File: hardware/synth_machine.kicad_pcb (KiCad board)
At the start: 2 copper layers, 100 x 100 mm, 93 parts, among them J1 USB-C (MIDI + 5V power), J10 Pot WAV (10k lin, panel) JST-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, J11 Pot ATK (10k lin, panel) JST-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, J12 Pot DEC (10k lin, panel) JST-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, J13 Pot SUS (10k lin, panel) JST-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, J14 Pot REL (10k lin, panel) JST-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, J5 Speaker L (JST-PH), J6 Speaker R (JST-PH), J7 Headphones 3.5mm (CUI SJ1-351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, J8 Expansion, K1 KEY C4 (direct D10) JST-XH, K10 A4 [c2 r2] JST-XH, K11 A#4 [c1 r1] JST-XH, K12 B4 [c1 r2] JST-XH, K13 C5 [c0 r2] JST-XH, K14 BTN1 [c0 r0] JST-XH, K15 BTN2 [c0 r1] JST-XH, K16 BTN3 [c1 r0] JST-XH, K17 BTN4 [c2 r0] JST-XH, K18 BTN5 [c3 r0] JST-XH, K19 BTN6 [c4 r0] JST-XH, K2 C#4 [c5 r0] JST-XH, K3 D4 [c5 r1] JST-XH, K4 D#4 [c4 r1] JST-XH, K5 E4 [c5 r2] JST-XH, K6 F4 [c4 r2] JST-XH, K7 F#4 [c3 r1] JST-XH, K8 G4 [c3 r2] JST-XH, K9 G#4 [c2 r1] JST-XH, Q1 MMBT3904, U1 Daisy Seed / Seed3, U2 TPA6138A2PWR, U3 MAX98306ETD+T

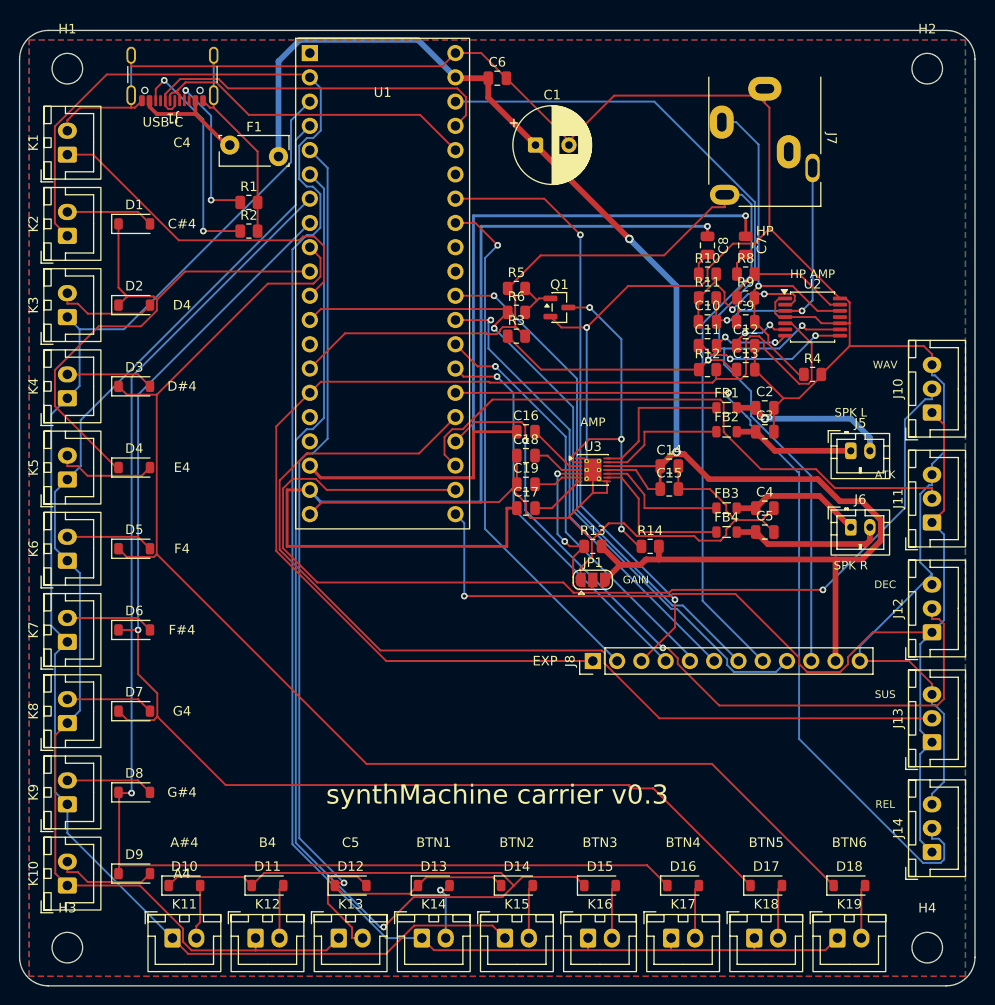
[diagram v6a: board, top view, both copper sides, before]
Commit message: v0.3 silkscreen tidy-up
- hide designators on holes, diodes, key/pot/speaker headers, USB-C, jack
  and expansion header; functional labels (key names, WAV..REL, SPK L/R,
  USB-C, HP, EXP) carry the silkscreen
- left-side matrix diodes rotated to sit parallel to their headers like the
  bottom row
- headphone-amp passives on a 5 x 3.5 mm grid, R4/R12/C13 pulled out of it
- expansion header centred under the Seed
- re-routed: 0 unrouted, DRC clean apart from known library nits

Co-Authored-By: Claude Fable 5.1 <noreply@anthropic.com>
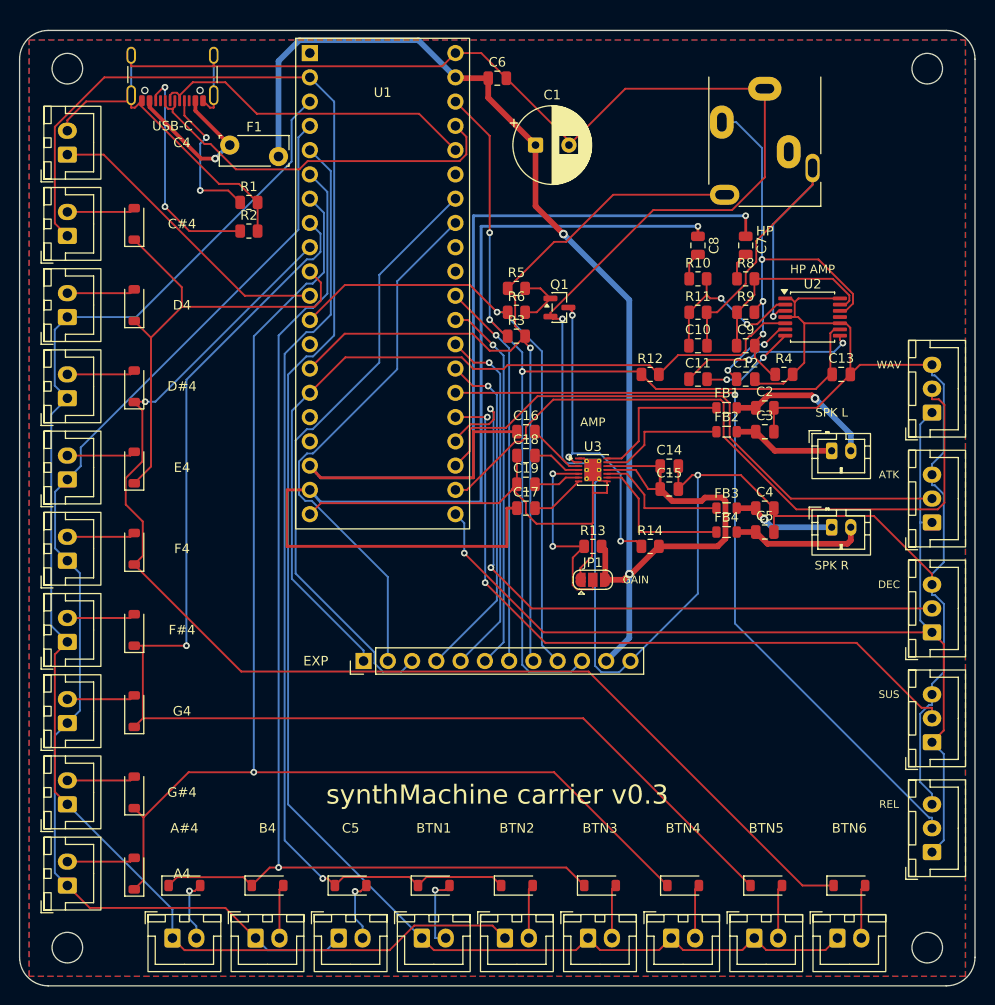
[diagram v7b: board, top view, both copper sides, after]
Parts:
- moved J8 24.0 mm to (36.0, 66.0)
- moved C13 10.0 mm to (86.0, 36.0)
- moved R12 6.02 mm to (66.0, 36.0)
- moved C11 3.64 mm to (71.0, 36.5)
- moved C12 3.50 mm to (76.0, 36.5)
- moved R4 3.00 mm to (80.0, 36.0)
- moved C10 2.69 mm to (71.0, 33.0)
- moved C9 2.50 mm to (76.0, 33.0)
- moved J5 2.00 mm to (85.0, 44.0)
- moved J6 2.00 mm to (85.0, 52.0)
- moved R11 1.80 mm to (71.0, 29.5)
- moved R9 1.50 mm to (76.0, 29.5)
- moved R10 1.12 mm to (71.0, 26.0)
- moved C8 1.00 mm to (71.0, 22.5)
- moved R8 0.50 mm to (76.0, 26.0)
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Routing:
- net GND: track 378.0 -> 418.1 mm, vias 1 -> 2
- net HP_MUTE: track 124.2 -> 87.2 mm
- net POT_WAVE: track 110.0 -> 75.7 mm, vias 1 -> 0
- net POT_SUSTAIN: track 104.6 -> 74.1 mm, vias 0 -> 2
- net COL1: track 146.5 -> 121.6 mm
- net +5V: track 170.5 -> 146.8 mm
- net HP_DET: track 112.5 -> 92.1 mm, vias 0 -> 1
- net +3V3: track 130.8 -> 110.8 mm, vias 2 -> 3
- net HP_R: track 29.1 -> 42.6 mm, vias 2 -> 1
- net MUTE: track 76.3 -> 62.9 mm
- net EXP_A8: track 53.5 -> 40.6 mm
- net EXP_A7: track 49.3 -> 39.4 mm
- net POT_RELEASE: track 92.9 -> 83.4 mm
- net POT_DECAY: track 80.5 -> 71.1 mm
- net +3.3VA: track 114.1 -> 107.1 mm
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
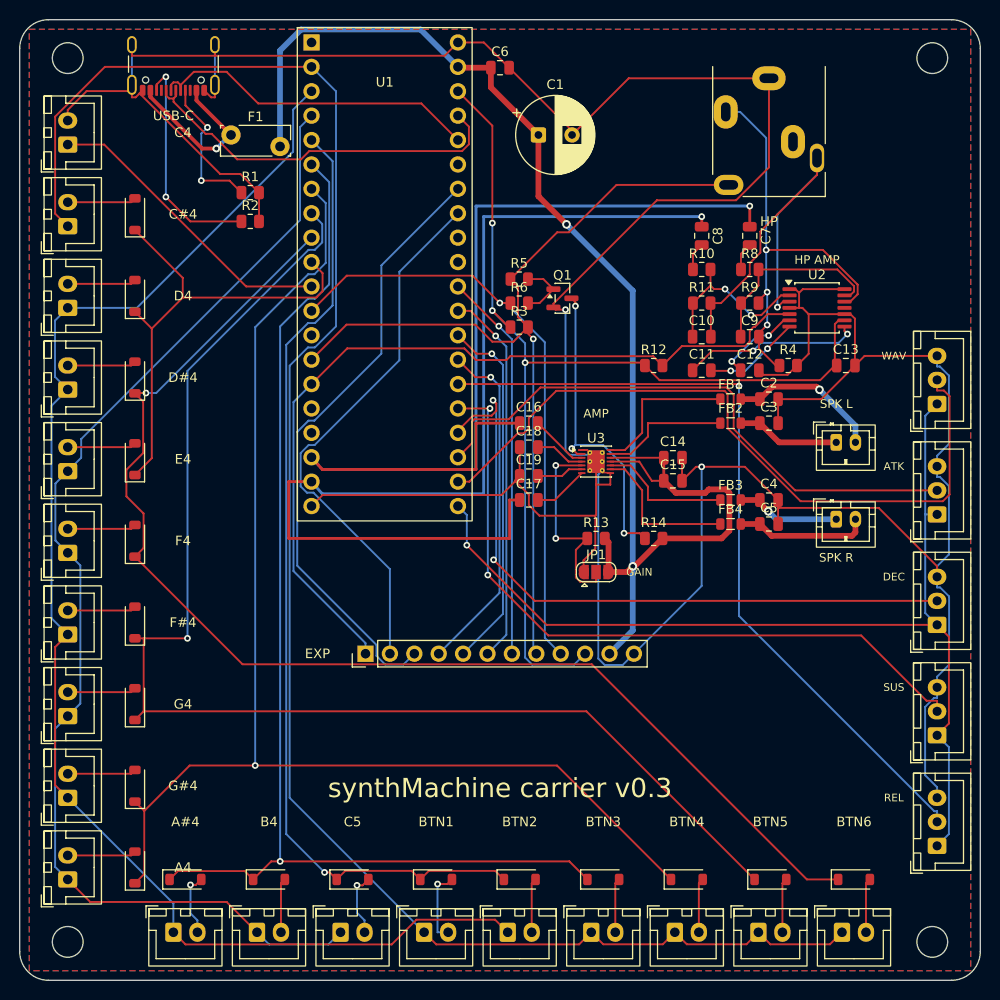
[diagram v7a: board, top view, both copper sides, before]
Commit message: v0.3 silkscreen: edge labels rotated to sit on the board edge, title moved up
Co-Authored-By: Claude Fable 5.1 <noreply@anthropic.com>
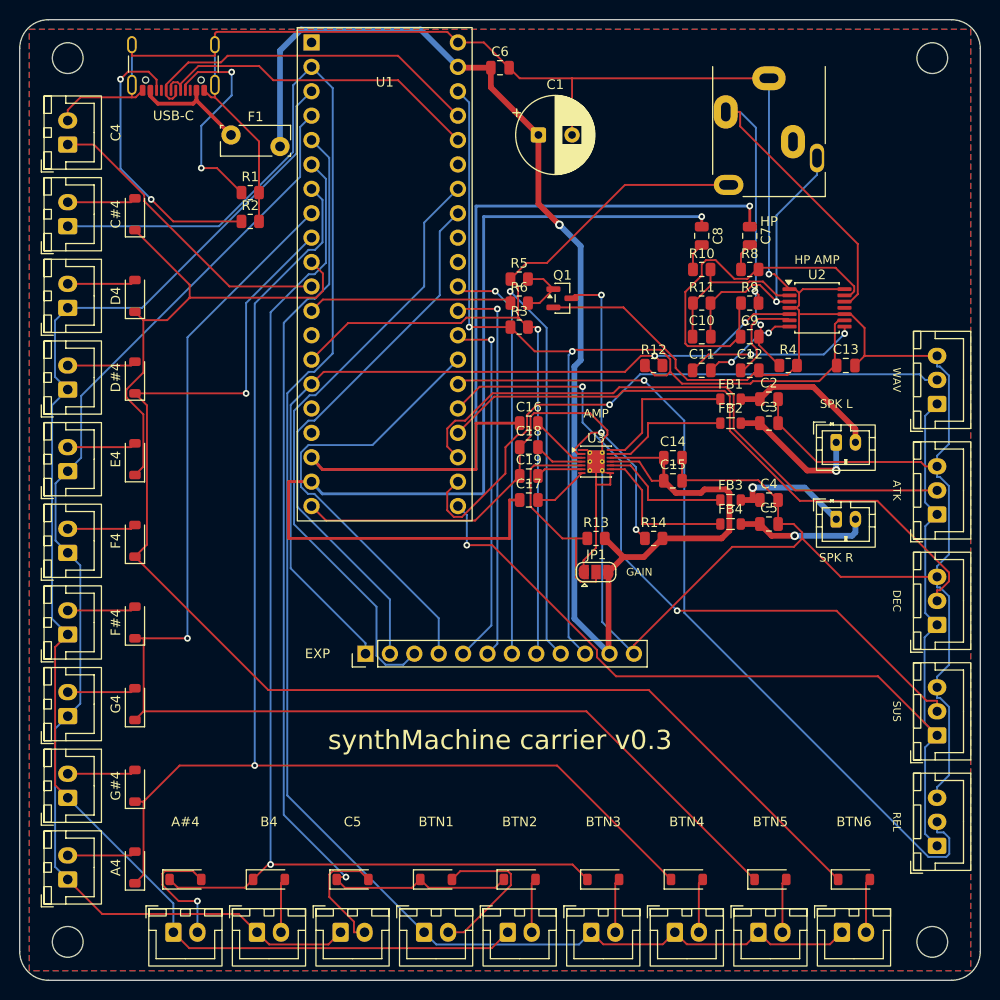
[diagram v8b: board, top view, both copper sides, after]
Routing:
- net HP_INL: track 20.1 -> 38.6 mm
- net HP_L: track 45.7 -> 58.5 mm, vias 3 -> 2
- net HP_R: track 42.6 -> 29.9 mm
- net POT_WAVE: track 75.7 -> 63.7 mm, vias 0 -> 1
- net EXP_A5: track 36.0 -> 47.6 mm, vias 1 -> 0
- net KBTN1_D: track 7.82 -> 16.3 mm, vias 1 -> 0
- net CC1: track 15.3 -> 22.5 mm
- net KAs4_D: track 6.59 -> 13.3 mm
- net +5V: track 146.8 -> 153.4 mm, vias 2 -> 1
- net CC2: track 23.3 -> 29.7 mm
- net KC5_D: track 6.65 -> 12.8 mm, vias 1 -> 0
- net VBUS: track 18.0 -> 12.0 mm, vias 1 -> 0
- net +3.3VA: track 107.1 -> 112.2 mm
- net ROW0: track 187.8 -> 183.2 mm
- net POT_DECAY: track 71.1 -> 66.5 mm, vias 2 -> 0
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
